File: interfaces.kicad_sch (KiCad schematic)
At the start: 19 parts, among them J2 Screw_Terminal_01x02, J4 Conn_01x05_Pin, J5 Conn_01x08_Pin, J6 Conn_01x02_Pin, Q1 2N7002, Q2 2N7002

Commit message: add gitignore
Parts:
- K1: value ~ -> (none)
- renumbered J5 to J1, J4 to J2, J6 to J5, J2 to J6, J2 to J7

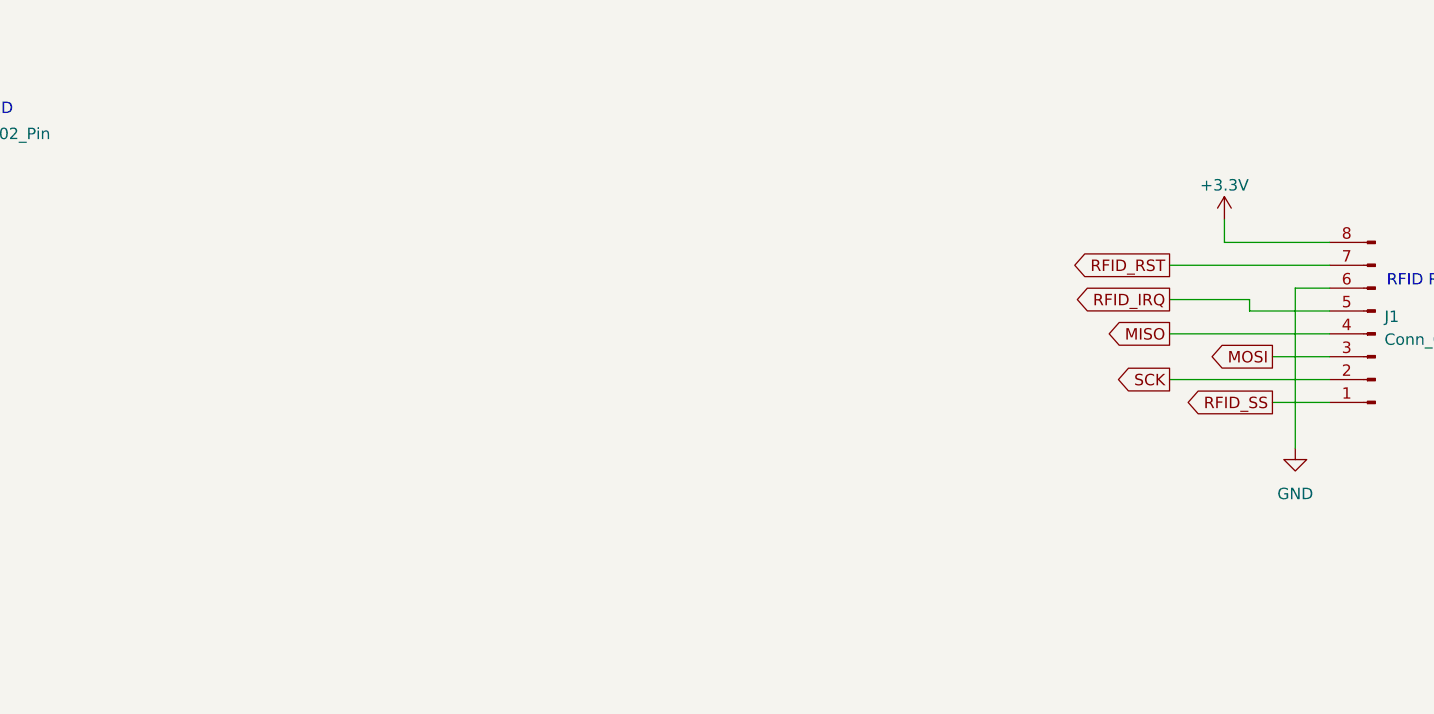
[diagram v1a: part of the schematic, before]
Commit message: Adapted gitignore Add LAN Add USB2RS232
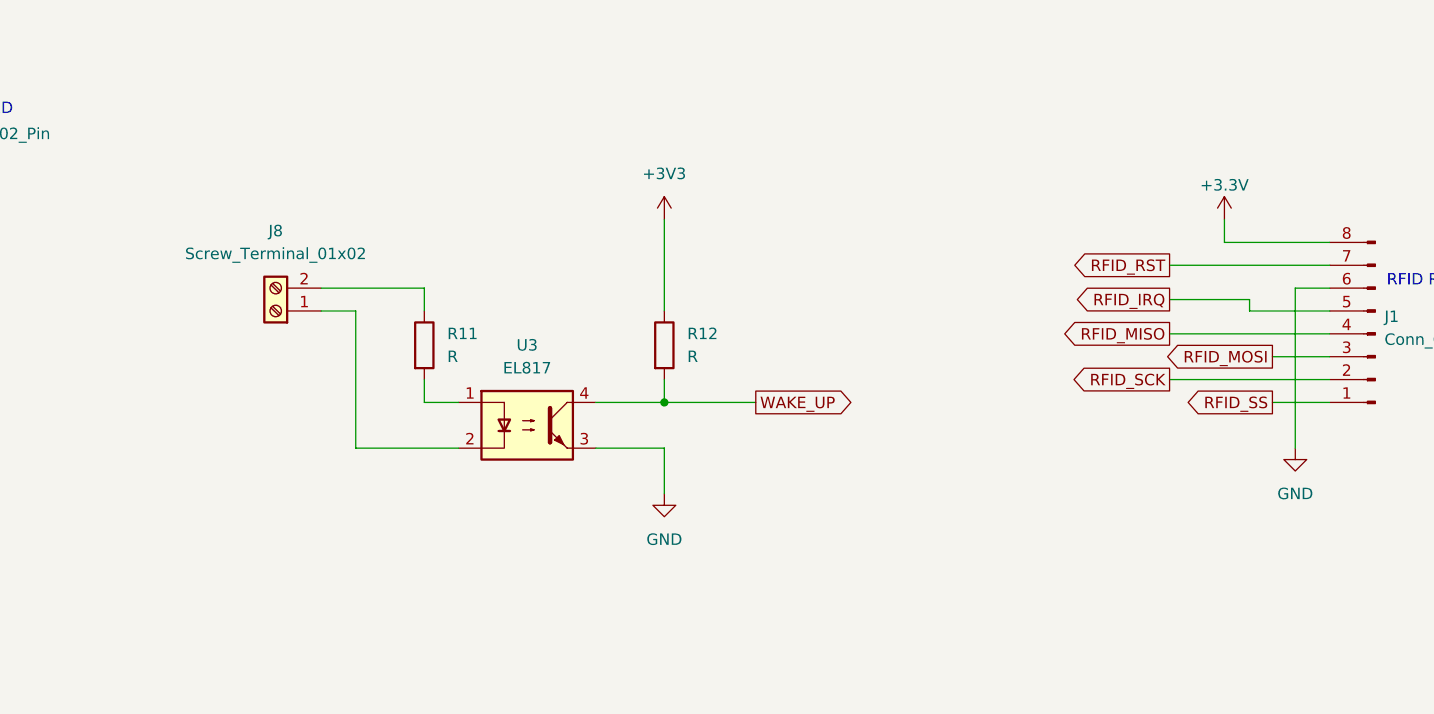
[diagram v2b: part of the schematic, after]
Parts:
- added J8: Screw_Terminal_01x02, Connector_Phoenix_MSTB:PhoenixContact_MSTBA_2,5_2-G-5,08_1x02_P5.08mm_Horizontal, symbol Connector:Screw_Terminal_01x02
- added R11, R12: R, Resistor_SMD:R_0603_1608Metric_Pad0.98x0.95mm_HandSolder, symbol Device:R
- added U3: EL817, Package_SO:SOP-4_3.8x4.1mm_P2.54mm, symbol Isolator:EL817
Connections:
- net GND: now also U3.3
- net MISO renamed RFID_MISO
- net MOSI renamed RFID_MOSI
- net SCK renamed RFID_SCK
- new net: J8.1 (Pin_1), U3.2
- new net: J8.2 (Pin_2), R11.1
- new net: R11.2, U3.1
- new net +3V3: R12.1
- new net WAKE_UP: R12.2, U3.4

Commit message: Connect W5500 to ESP32, fix RFID SCK, add relay flyback diode
- ESP32: add global labels LAN_CS/RST/INT/SCK/MISO/MOSI on GPIO 5/6/7/14/15/16
  (matches WIRING_OVERVIEW.md)
- ESP32: rename SCK label to RFID_SCK so GPIO12 reaches PN532 connector J1
- ESP32: connect WAKE_UP (optocoupler U3) to GPIO21
- LAN: power WIZ850io from +3.3V instead of unconnected +3V3 net
- Interfaces: add flyback diode D5 (1N4148W, LCSC C81598) across K1 coil
- Interfaces: tie R12 pull-up to +3.3V, set value to 10k
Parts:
- added D5: 1N4148W, Diode_SMD:D_SOD-123, symbol Device:D
- R12: value R -> 10k
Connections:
- net +3V3 is gone; now on net +3.3V: R12.1
- net +5V: now also D5.1 (K)
- net at K1.10, Q2.3 (D): now also D5.2 (A)
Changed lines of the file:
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@@
+	(wire
+		(pts
+			(xy 69.85 45.72) (xy 69.85 49.53)
+		)
+		(stroke
+			(width 0)
+			(type default)
+		)
+	)
 	(wire
 		(pts
@@
 	(wire
 		(pts
+			(xy 69.85 38.1) (xy 69.85 34.29)
+		)
+		(stroke
+			(width 0)
+			(type default)
+		)
+	)
+	(wire
+		(pts
 			(xy 45.72 158.75) (xy 33.02 158.75)
 		)
@@
 	(wire
 		(pts
+			(xy 69.85 49.53) (xy 80.01 49.53)
+		)
+		(stroke
+			(width 0)
+			(type default)
+		)
+	)
+	(wire
+		(pts
 			(xy 45.72 153.67) (xy 40.64 153.67)
 		)
@@
 		(pts
 			(xy 237.744 115.57) (xy 244.094 115.57)
+		)
+		(stroke
+			(width 0)
+			(type default)
+		)
+	)
+	(wire
+		(pts
+			(xy 69.85 34.29) (xy 80.01 34.29)
 		)
 		(stroke
@@
 			)
 		)
-		(property "Value" "+3V3"
-			(at 170.18 95.25 0)
-			(show_name no)
-			(do_not_autoplace no)
-			(effects
-				(font
-					(size 1.27 1.27)
-				)
+		(property "Value" "+3.3V"
+			(at 172.72 99.0599 0)
+			(show_name no)
+			(do_not_autoplace no)
+			(effects
+				(font
+					(size 1.27 1.27)
+				)
+				(justify left)
 			)
 		)
@@
 			)
 		)
-		(property "Value" "R"
+		(property "Value" "10k"
 			(at 172.72 115.5699 0)
 			(show_name no)
@@
 					(unit 1)
 				)
+			)
+		)
+	)
+	(symbol
+		(lib_id "Device:D")
+		(at 69.85 41.91 270)
+		(unit 1)
+		(body_style 1)
+		(exclude_from_sim no)
+		(in_bom yes)
+		(on_board yes)
+		(in_pos_files yes)
+		(dnp no)
+		(property "Reference" "D5"
+			(at 67.31 41.91 0)
+			(show_name no)
+			(do_not_autoplace no)
+			(effects
+				(font
+					(size 1.27 1.27)
+				)
+			)
+		)
+		(property "Value" "1N4148W"
+			(at 72.39 41.91 0)
+			(show_name no)
+			(do_not_autoplace no)
+			(effects
+				(font
+					(size 1.27 1.27)
+				)
+			)
+		)
+		(property "Footprint" "Diode_SMD:D_SOD-123"
+			(at 69.85 41.91 0)
+			(hide yes)
+			(show_name no)
+			(do_not_autoplace no)
+			(effects
+				(font
+					(size 1.27 1.27)
+				)
+			)
+		)
+		(property "Datasheet" ""
+			(at 69.85 41.91 0)
+			(hide yes)
+			(show_name no)
+			(do_not_autoplace no)
+			(effects
+				(font
+					(size 1.27 1.27)
+				)
+			)
+		)
+		(property "Description" "Diode"
+			(at 69.85 41.91 0)
+			(hide yes)
+			(show_name no)
+			(do_not_autoplace no)
+			(effects
+				(font
+					(size 1.27 1.27)
+				)
+			)
+		)
+    (property "LCSC" "C81598" (at 69.85 41.91 0)
+      (effects (font (size 1.27 1.27)) (hide yes))
+    )
+		(pin "1"
+		)
+		(pin "2"
+		)
+		(instances
+			(project "GA_Fuelstation_Terminal"
+				(path "/9d5c9b65-fa9a-4f2b-b8e4-a4447f224f28/3fe47dfa-b184-478e-8a53-8cc5e5cfa822"
+					(reference "D5")
+					(unit 1)
+				)

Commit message: Add input protection, fix USB-C/CP2102 supply, harden optocoupler input
Power supply:
- Add 12V input protection: PTC fuse F1 (1.1A/33V, C70119), TVS D6
  (SMAJ15CA, C151939), reverse polarity Schottky D7 (SS34, C8678) and
  bulk cap C13 (100uF/25V, C179802)

USB2RS232:
- Power CP2102N (VDD/REGIN) from +3.3V via R25 (0R)
- Add 5k1 pull-downs R23/R24 on USB-C CC1/CC2 so C-to-C hosts supply VBUS

ESP32 / Interfaces:
- Add 100k gate pull-downs R26/R27/R28 on Q2/Q1/Q3 (relay, LED, buzzer
  stay off during reset/boot)
- Buzzer flyback D1: 1N4148W SOD-123 (C81598) instead of undefined SOT-23
- WAKE_UP input (J8/U3): series zener D8 (BZT52C6V8, C173404), reverse
  polarity diode D9 (1N4148W), R11 = 1k5 0805 (C4310); switches at ~9V,
  safe up to 14.4V
- IC1 value set to ESP32-S3-WROOM-1U to match footprint
- Add no-connect flags on unused ESP32, J99 and K1 pins
- Remove duplicate local labels IO_PUMP_LED/IO_PUMP_RELAIS
- Move off-grid symbols, labels and wires onto grid

PCB: update from schematic
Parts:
- added D8: BZT52C6V8, Diode_SMD:D_SOD-123, symbol Device:D_Zener
- added D9: 1N4148W, Diode_SMD:D_SOD-123, symbol Device:D
- added R26, R27: 100k, Resistor_SMD:R_0402_1005Metric_Pad0.72x0.64mm_HandSolder, symbol Device:R
- R11: value R -> 1k5; footprint Resistor_SMD:R_0603_1608Metric_Pad0.98x0.95mm_HandSolder -> Resistor_SMD:R_0805_2012Metric_Pad1.20x1.40mm_HandSolder; LCSC (none) -> C4310
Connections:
- net GND: now also R26.2, R27.2
- net at Q1.1 (G), R4.2: now also R27.1
- net at Q2.1 (G), R5.2: now also R26.1
- net at J8.1 (Pin_1), U3.2: now also D9.2 (A)
- net at J8.2 (Pin_2): now also D8.1 (K); no longer R11.1
- net at R11.2, U3.1: now also D9.1 (K)
- new net: D8.2 (A), R11.1
- no-connect marks 0 -> 4
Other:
- moved on the sheet: J1, R8

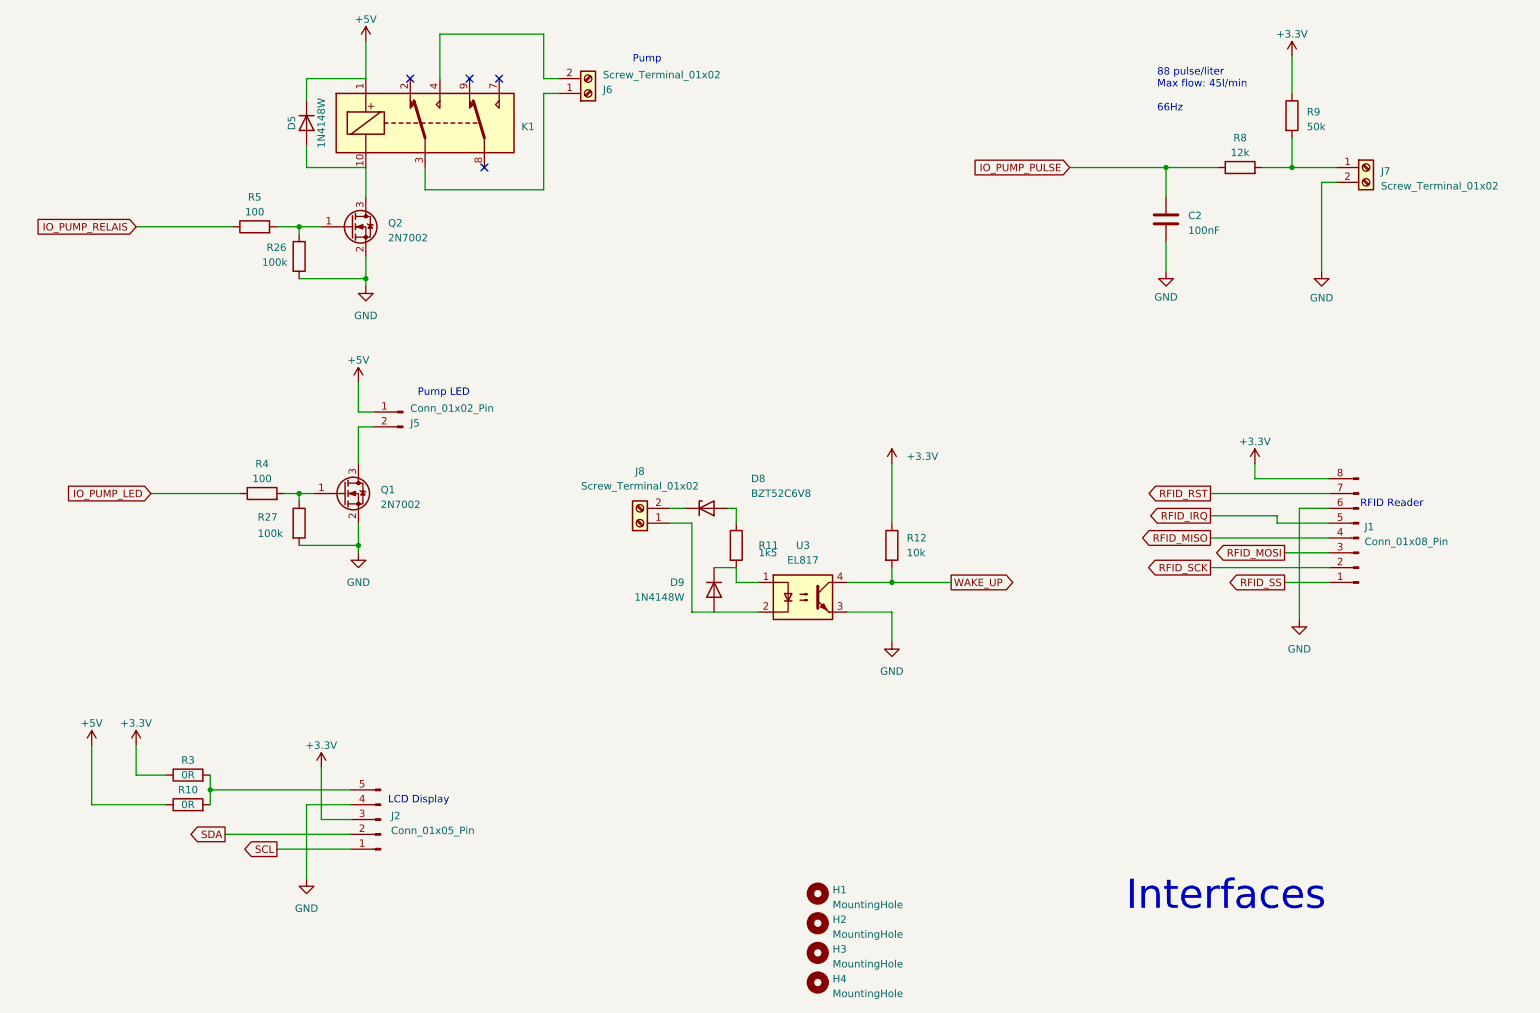
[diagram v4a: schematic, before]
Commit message: Add native ESP32-S3 USB port, move buzzer driver to Interfaces sheet
ESP32:
- Add USB-C J4 for ESP32-S3 native USB (USB-Serial-JTAG):
  D+ -> GPIO20, D- -> GPIO19 via 0R series resistors R31/R32 (0402, C17168),
  ESD diodes D10/D12 (LESD5D5.0CT1G), CC pull-downs R29/R30 5k1,
  VBUS not connected (no-connect flag)
- Move JTAG header J99 and decoupling C10-C12 to free space for J4

Interfaces:
- Move buzzer driver (Q3, R6, R28, R2, R7, D1, BZ1) from ESP32 sheet
- Make IO_BUZZER a global label so GPIO4 still reaches R6/Q3
- Shift optocoupler input block (J8, D8, D9, R11, R12, U3) down

Power supply:
- Add PWR_FLAG on +12V after reverse polarity diode D7 (ERC clean)

PCB: update from schematic
ERC: 0 errors, 5 warnings (2N7002 symbol lib mismatch, unused RFID_IRQ/RST)
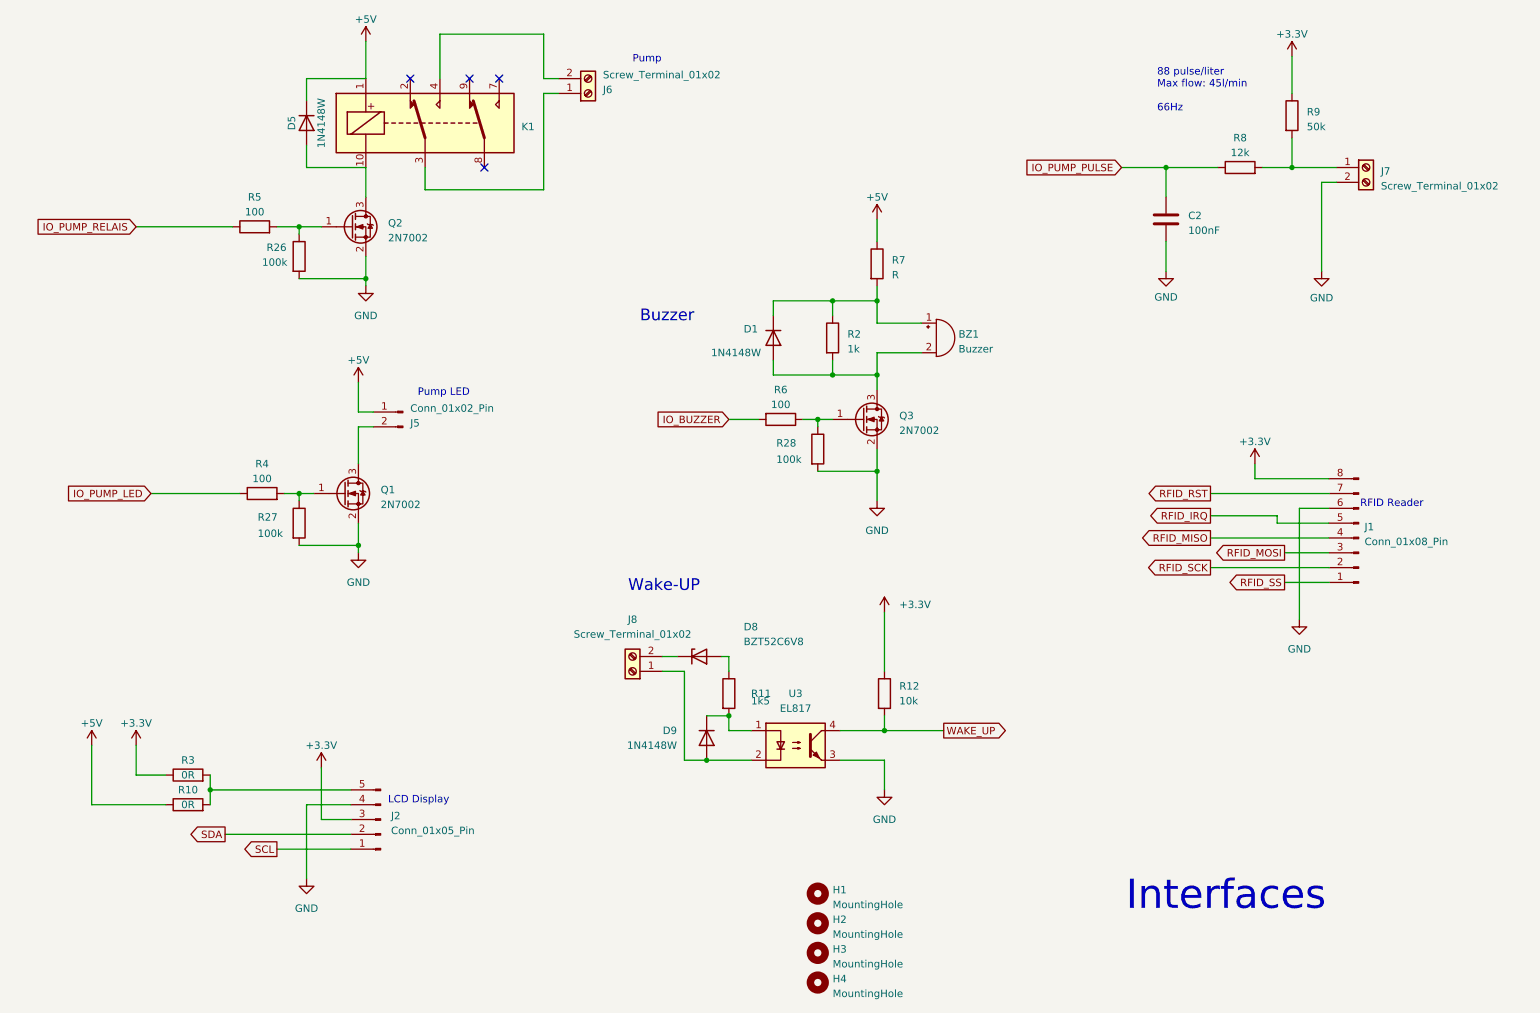
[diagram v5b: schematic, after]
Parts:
- added BZ1: Buzzer, GA_Fuelstation_Terminal:8530-SMD, symbol Device:Buzzer
- added D1: 1N4148W, Diode_SMD:D_SOD-123, symbol Device:D
- added Q3: 2N7002, Package_TO_SOT_SMD:SOT-23, symbol Transistor_FET:2N7002
- added R2: 1k, Resistor_SMD:R_0805_2012Metric_Pad1.20x1.40mm_HandSolder, symbol Device:R
- added R28: 100k, Resistor_SMD:R_0402_1005Metric_Pad0.72x0.64mm_HandSolder, symbol Device:R
- added R6: 100, Resistor_SMD:R_0805_2012Metric_Pad1.20x1.40mm_HandSolder, symbol Device:R
- added R7: R, Resistor_SMD:R_0805_2012Metric_Pad1.20x1.40mm_HandSolder, symbol Device:R
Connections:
- net +5V: now also R7.1
- net GND: now also Q3.2 (S), R28.2
- new net: Q3.1 (G), R28.1, R6.1
- new net: BZ1.1 (-), D1.1 (K), R2.1, R7.2
- new net: BZ1.2 (+), D1.2 (A), Q3.3 (D), R2.2
- new net IO_BUZZER: R6.2
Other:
- note added: "Buzzer"
- note added: "Wake-UP"
- moved on the sheet: D8, D9, J8, R11, R12, U3
